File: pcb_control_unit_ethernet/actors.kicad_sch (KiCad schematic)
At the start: 51 parts, among them J17 STEP1, J18 STEP2, J19 Conveyor, J20 Valve, J21 Bus-Servo, J22 Compressor, Q1 IRLML6344, Q2 IRLML6344, Q3 IRLML6344, U7 TMC2209, U8 TMC2209

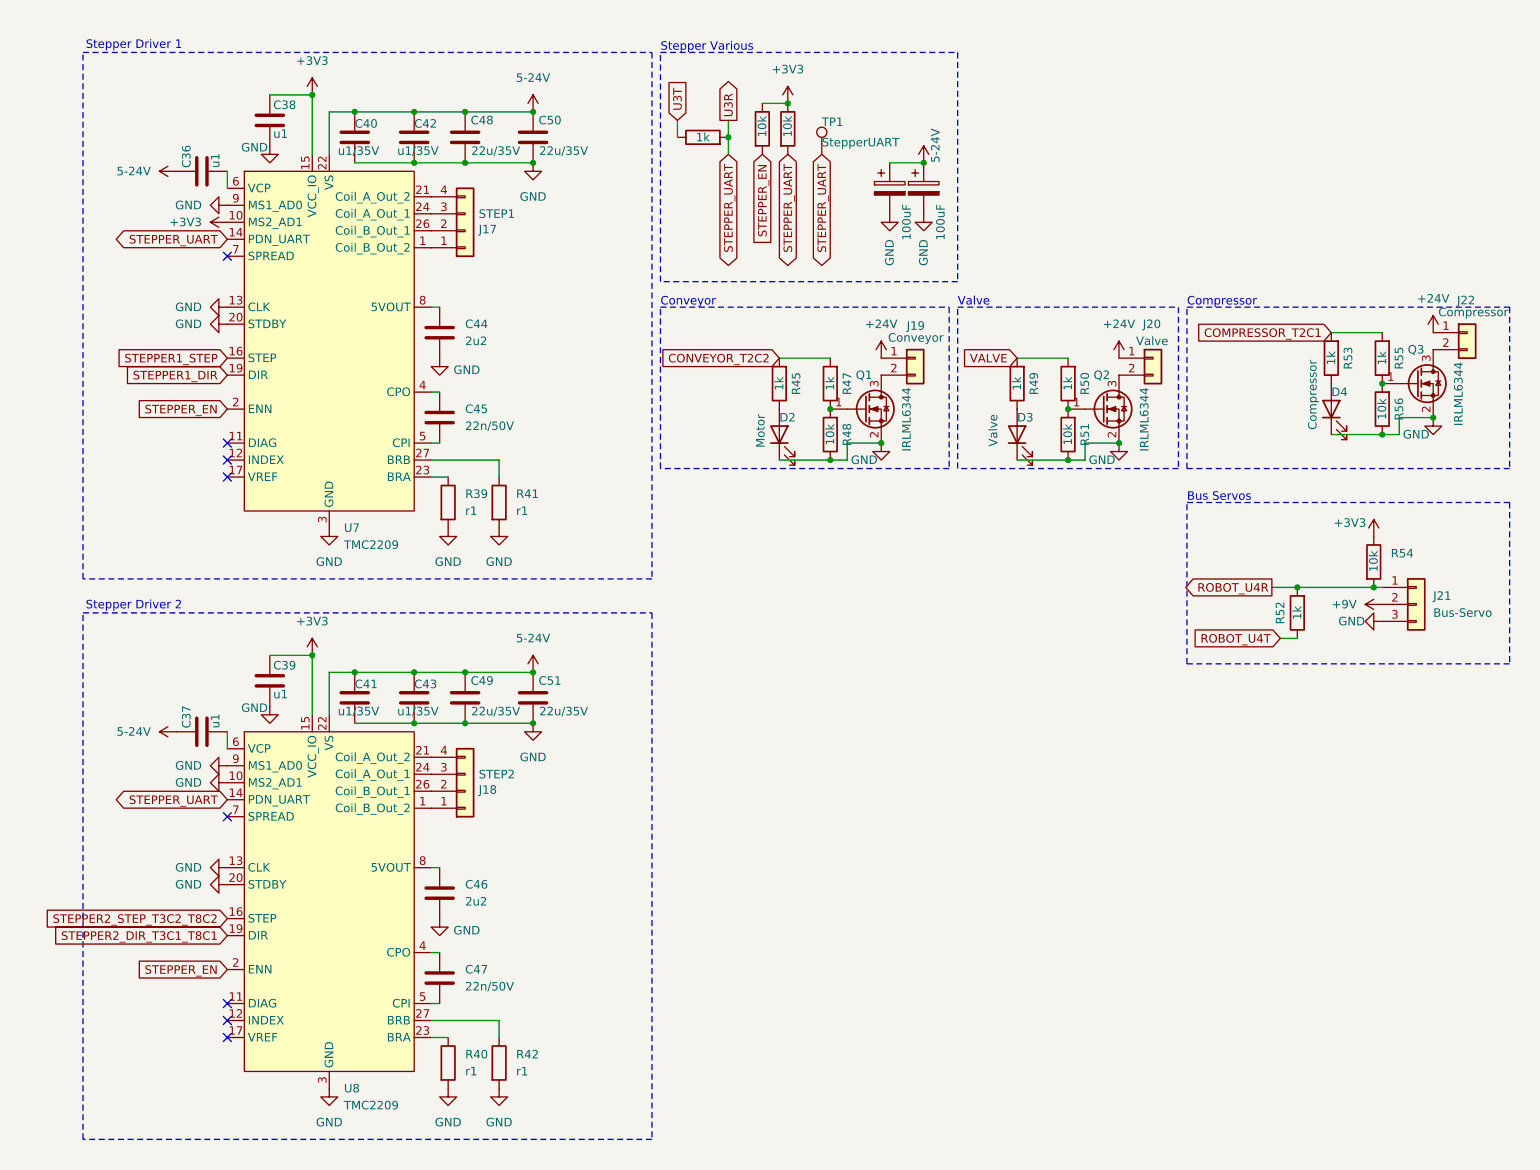
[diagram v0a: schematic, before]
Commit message: First time zero errors, but bad layout
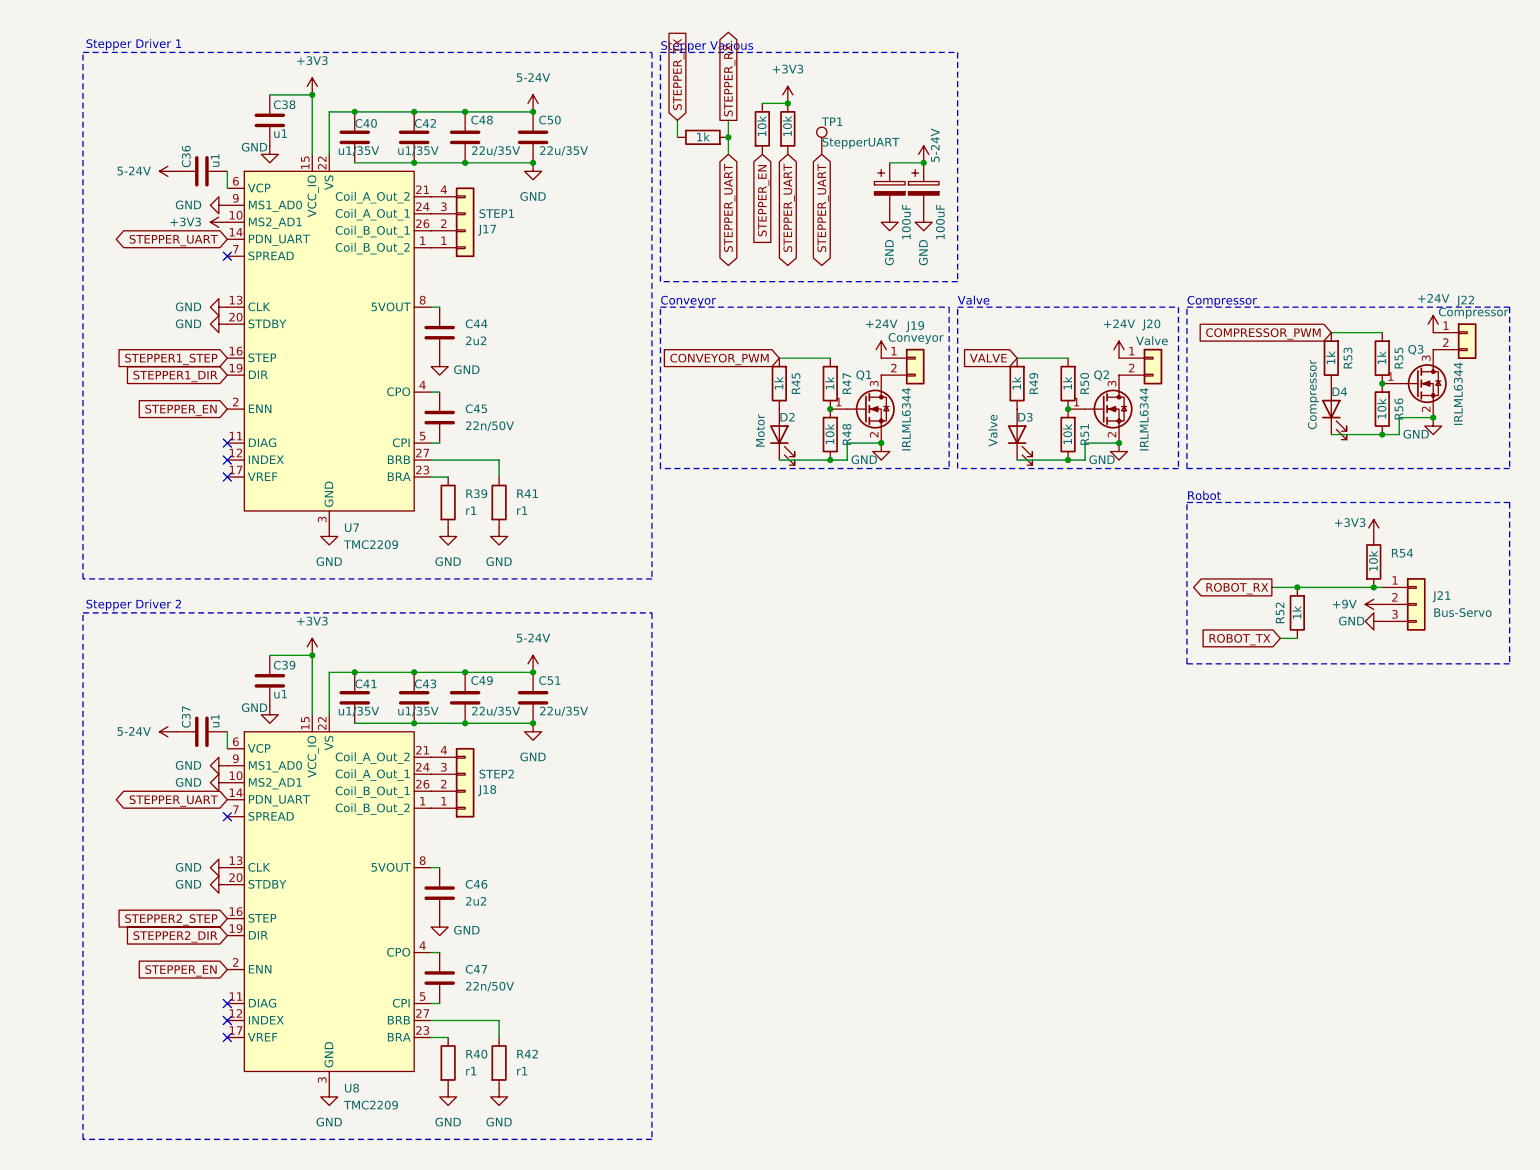
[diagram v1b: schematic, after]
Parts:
- C52, C53: footprint Capacitor_THT:CP_Radial_D8.0mm_P2.50mm -> Capacitor_SMD:CP_Elec_6.3x7.7
- R44, R46: footprint Resistor_SMD:R_0402_1005Metric -> Resistor_SMD:R_0201_0603Metric
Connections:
- net COMPRESSOR_T2C1 renamed COMPRESSOR_PWM
- net CONVEYOR_T2C2 renamed CONVEYOR_PWM
- net ROBOT_U4R renamed ROBOT_RX
- net ROBOT_U4T renamed ROBOT_TX
- net STEPPER2_DIR_T3C1_T8C1 renamed STEPPER2_DIR
- net STEPPER2_STEP_T3C2_T8C2 renamed STEPPER2_STEP
- net STEPPER_UART renamed STEPPER_RX
- net U3T renamed STEPPER_TX
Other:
- note added: "Robot"
- note removed: "Bus Servos"
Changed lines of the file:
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@@
 		)
 	)
-	(text "Bus Servos"
+	(text "Robot"
 		(exclude_from_sim no)
 		(at 187.96 83.82 0)
@@
 	)
 	(junction
-		(at 148.59 33.02)
-		(diameter 0)
-		(color 0 0 0 0)
-	)
-	(junction
 		(at 90.17 25.4)
 		(diameter 0)
@@
 	)
 	(junction
+		(at 148.59 33.02)
+		(diameter 0)
+		(color 0 0 0 0)
+	)
+	(junction
 		(at 72.39 109.22)
 		(diameter 0)
@@
 		)
 	)
-	(global_label "STEPPER2_DIR_T3C1_T8C1"
+	(global_label "STEPPER2_DIR"
 		(shape input)
 		(at 44.45 148.59 180)
@@
 		)
 		(property "Intersheetrefs" "${INTERSHEET_REFS}"
-			(at 16.6094 148.59 0)
+			(at 27.8578 148.59 0)
 			(effects
 				(font
@@
 		)
 	)
-	(global_label "ROBOT_U4T"
+	(global_label "ROBOT_TX"
 		(shape input)
 		(at 201.93 104.14 180)
@@
 		)
 		(property "Intersheetrefs" "${INTERSHEET_REFS}"
-			(at 188.301 104.14 0)
+			(at 189.6315 104.14 0)
 			(effects
 				(font
@@
 		)
 	)
-	(global_label "STEPPER2_STEP_T3C2_T8C2"
+	(global_label "STEPPER2_STEP"
 		(shape input)
 		(at 44.45 146.05 180)
@@
 		)
 		(property "Intersheetrefs" "${INTERSHEET_REFS}"
-			(at 15.1581 146.05 0)
+			(at 26.4065 146.05 0)
 			(effects
 				(font
@@
 		)
 	)
-	(global_label "COMPRESSOR_T2C1"
+	(global_label "COMPRESSOR_PWM"
 		(shape input)
 		(at 209.55 58.42 180)
@@
 		)
 		(property "Intersheetrefs" "${INTERSHEET_REFS}"
-			(at 188.1802 58.42 0)
+			(at 188.664 58.42 0)
 			(effects
 				(font
@@
 		)
 	)
-	(global_label "U3R"
+	(global_label "STEPPER_RX"
 		(shape output)
 		(at 119.38 26.67 90)
@@
 		)
 		(property "Intersheetrefs" "${INTERSHEET_REFS}"
-			(at 119.38 19.8748 90)
+			(at 119.38 11.9526 90)
 			(effects
 				(font
@@
 		)
 	)
-	(global_label "CONVEYOR_T2C2"
+	(global_label "CONVEYOR_PWM"
 		(shape input)
 		(at 127 62.23 180)
@@
 		)
 		(property "Intersheetrefs" "${INTERSHEET_REFS}"
-			(at 108.5329 62.23 0)
+			(at 109.0167 62.23 0)
 			(effects
 				(font
@@
 		)
 	)
-	(global_label "ROBOT_U4R"
+	(global_label "ROBOT_RX"
 		(shape output)
 		(at 200.66 96.52 180)
@@
 		)
 		(property "Intersheetrefs" "${INTERSHEET_REFS}"
-			(at 186.7286 96.52 0)
+			(at 188.0591 96.52 0)
 			(effects
 				(font
@@
 		)
 	)
-	(global_label "U3T"
+	(global_label "STEPPER_TX"
 		(shape input)
 		(at 111.76 26.67 90)
@@
 		)
 		(property "Intersheetrefs" "${INTERSHEET_REFS}"
-			(at 111.76 20.1772 90)
+			(at 111.76 12.255 90)
 			(effects
 				(font
@@
 	)
 	(symbol
+		(lib_id "Device:C_Polarized")
+		(at 148.59 36.83 0)
+		(unit 1)
+		(exclude_from_sim no)
+		(in_bom yes)
+		(on_board yes)
+		(dnp no)
+		(property "Reference" "C53"
+			(at 156.21 35.941 90)
+			(effects
+				(font
+					(size 1.27 1.27)
+				)
+				(hide yes)
+			)
+		)
+		(property "Value" "100uF"
+			(at 151.13 41.91 90)
+			(effects
+				(font
+					(size 1.27 1.27)
+				)
+			)
+		)
+		(property "Footprint" "Capacitor_SMD:CP_Elec_6.3x7.7"
+			(at 149.5552 40.64 0)
+			(effects
+				(font
+					(size 1.27 1.27)
+				)
+				(hide yes)
+			)
+		)
+		(property "Datasheet" "C72478"
+			(at 148.59 36.83 0)
+			(effects
+				(font
+					(size 1.27 1.27)
+				)
+				(hide yes)
+			)
+		)
+		(property "Description" "Polarized capacitor"
+			(at 148.59 36.83 0)
+			(effects
+				(font
+					(size 1.27 1.27)
+				)
+				(hide yes)
+			)
+		)
+		(pin "2"
+		)
+		(pin "1"
+		)
+		(instances
+			(project "pcb_control_unit_ethernet"
+				(path "/9c57264a-0988-4c94-95c0-340e4ca73bd5/3e57726e-e70f-48f8-bf8b-be1a55c6b2d5"
+					(reference "C53")
+					(unit 1)
+				)
+			)
+		)
+	)
+	(symbol
 		(lib_id "power:+VSW")
 		(at 36.83 118.11 90)
@@
 			)
 		)
-		(property "Footprint" "Resistor_SMD:R_0402_1005Metric"
+		(property "Footprint" "Resistor_SMD:R_0201_0603Metric"
 			(at 126.492 27.94 90)
 			(effects
@@
 	)
 	(symbol
-		(lib_id "Device:C_Polarized")
-		(at 148.59 36.83 0)
-		(unit 1)
-		(exclude_from_sim no)
-		(in_bom yes)
-		(on_board yes)
-		(dnp no)
-		(property "Reference" "C53"
-			(at 156.21 35.941 90)
-			(effects
-				(font
-					(size 1.27 1.27)
-				)
-				(hide yes)
-			)
-		)
-		(property "Value" "100uF"
-			(at 151.13 41.91 90)
-			(effects
-				(font
-					(size 1.27 1.27)
-				)
-			)
-		)
-		(property "Footprint" "Capacitor_THT:CP_Radial_D8.0mm_P2.50mm"
-			(at 149.5552 40.64 0)
-			(effects
-				(font
-					(size 1.27 1.27)
-				)
-				(hide yes)
-			)
-		)
-		(property "Datasheet" "~"
-			(at 148.59 36.83 0)
-			(effects
-				(font
-					(size 1.27 1.27)
-				)
-				(hide yes)
-			)
-		)
-		(property "Description" "Polarized capacitor"
-			(at 148.59 36.83 0)
-			(effects
-				(font
-					(size 1.27 1.27)
-				)
-				(hide yes)
-			)
-		)
-		(pin "2"
-		)
-		(pin "1"
-		)
-		(instances
-			(project "pcb_control_unit_ethernet"
-				(path "/9c57264a-0988-4c94-95c0-340e4ca73bd5/3e57726e-e70f-48f8-bf8b-be1a55c6b2d5"
-					(reference "C53")
-					(unit 1)
-				)
-			)
-		)
-	)
-	(symbol
 		(lib_id "Connector_Generic:Conn_01x02")
 		(at 229.87 58.42 0)
@@
 			)
 		)
-		(property "Footprint" "Resistor_SMD:R_0402_1005Metric"
+		(property "Footprint" "Resistor_SMD:R_0201_0603Metric"
 			(at 122.682 27.94 90)
 			(effects
@@
 			)
 		)
-		(property "Footprint" "Capacitor_THT:CP_Radial_D8.0mm_P2.50mm"
+		(property "Footprint" "Capacitor_SMD:CP_Elec_6.3x7.7"
 			(at 144.4752 40.64 0)
 			(effects
@@
 			)
 		)
-		(property "Datasheet" "~"
+		(property "Datasheet" "C72478"
 			(at 143.51 36.83 0)
 			(effects

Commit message: WIP
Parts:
- added C62: u1, Capacitor_SMD:C_0402_1005Metric, symbol Device:C
- added U11: 74AHCT125, Package_SO:SOIC-14_3.9x8.7mm_P1.27mm, symbol 74xx:74AHCT125
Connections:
- net GND: now also C62.2, U11.1, U11.10, U11.12, U11.13, U11.4, U11.7 (GND), U11.9
- new net +5V: C62.1, U11.14 (VCC)
- new net T15C1: U11.2
- new net T15C2: U11.5
- new net WS2812_CH1: U11.3
- new net WS2812_CH2: U11.6
- no-connect marks 8 -> 10
